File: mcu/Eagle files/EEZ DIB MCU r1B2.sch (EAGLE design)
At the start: 189 parts, among them IC1 TPD4E001DRLR, IC10 TPS2051BDBVR, IC11 TPS61169DCKR, IC12 TPD4E001DRLR, IC13 TPA6205A1DGN, IC14 TPD4E001DRLR, IC15 AR1021-I/SS, IC16 TPD4E001DRLR, IC17 DP83848CVV/NOPB, IC2 SN74LVC2G34DBVR, IC3 BTS3408G, IC4 STM32F769IGT6, IC5 LD1117ADT33TR, IC6 TPD4E001DRLR, IC7 TPD4E001DRLR, IC8 IS42S16400J, IC9 BR24G64FVT-3AGE2, J1 5033981892, Q1 MMBT5551, SW1 PEC16-2215F-S0024, SW2 BSF-3152, X1 ZL263-40DG, X2 ZL231-16KG, X3 1844249, X4 ZL231-20KG, X5 292304-1, X6 LMJTAB881243M-L, Y1 10MHz

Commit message: #3
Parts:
- removed X5: 292304-1, EEZ_Lib1:USB-B292304-1
- added J2: 678038020, EEZ_Lib1:678038020
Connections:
- net GND: now also J2.GND
- net PE: now also J2.SH1, J2.SH2; no longer X5.SHIELD
- net USB_D_N: now also J2.D-; no longer X5.2
- net USB_D_P: now also IC12.IO2, J2.D+; no longer IC12.IO3, X5.3
- net USB_OTG_FS_ID: now also IC12.IO3, J2.ID; no longer X5.4
- net USB_OTG_FS_VBUS: now also J2.VCC; no longer X5.1
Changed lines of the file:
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@@
 <?xml version="1.0" encoding="utf-8"?>
 <!DOCTYPE eagle SYSTEM "eagle.dtd">
-<eagle version="9.1.0">
+<eagle version="7.2.0">
 <drawing>
 <settings>
 <setting alwaysvectorfont="no"/>
-<setting keepoldvectorfont="yes"/>
 <setting verticaltext="up"/>
 </settings>
@@
 <part name="C22" library="rcl" deviceset="C-EU" device="C0603" value="N.C."/>
 <part name="SUPPLY3" library="supply2" deviceset="GND" device=""/>
-<part name="X5" library="EEZ_Lib1" deviceset="USB-B" device="292304-1" value="292304-1"/>
 <part name="PE3" library="supply1" deviceset="PE" device=""/>
 <part name="X1" library="EEZ_connectors" deviceset="ZL263-40DG" device="" value="ZL263-40DG"/>
@@
 <part name="+3V12" library="supply1" deviceset="+3V3" device=""/>
 <part name="+3V14" library="supply1" deviceset="+3V3" device=""/>
+<part name="J2" library="EEZ_Lib1" deviceset="678038020" device=""/>
+<part name="SUPPLY21" library="supply2" deviceset="GND" device=""/>
 </parts>
 <sheets>
@@
 <attribute name="DRAWING_NAME" x="180.34" y="19.05" size="2.54" layer="94" font="vector"/>
 </instance>
-<instance part="X5" gate="G$1" x="241.3" y="134.62" smashed="yes">
-<attribute name="NAME" x="243.84" y="137.795" size="1.778" layer="95"/>
-<attribute name="VALUE" x="250.19" y="121.92" size="1.778" layer="96"/>
-</instance>
-<instance part="PE3" gate="M" x="248.92" y="116.84" smashed="yes">
-<attribute name="VALUE" x="246.38" y="117.475" size="1.778" layer="96" rot="R180"/>
+<instance part="PE3" gate="M" x="243.84" y="111.76" smashed="yes">
+<attribute name="VALUE" x="241.3" y="112.395" size="1.778" layer="96" rot="R180"/>
 </instance>
 <instance part="IC11" gate="A" x="45.72" y="152.4" smashed="yes">
@@
 <attribute name="VALUE" x="248.031" y="143.51" size="1.778" layer="96" rot="MR180"/>
 </instance>
+<instance part="J2" gate="G$1" x="251.46" y="129.54" smashed="yes">
+<attribute name="NAME" x="251.46" y="139.065" size="1.778" layer="95"/>
+<attribute name="VALUE" x="246.38" y="113.665" size="1.778" layer="96"/>
+</instance>
+<instance part="SUPPLY21" gate="GND" x="236.22" y="119.38" smashed="yes">
+<attribute name="VALUE" x="233.68" y="115.57" size="1.778" layer="96"/>
+</instance>
 </instances>
 <busses>
@@
 <segment>
 <pinref part="PE3" gate="M" pin="PE"/>
-<pinref part="X5" gate="G$1" pin="SHIELD"/>
-<wire x1="248.92" y1="119.38" x2="248.92" y2="121.92" width="0.1524" layer="91"/>
+<wire x1="243.84" y1="114.3" x2="243.84" y2="116.84" width="0.1524" layer="91"/>
+<pinref part="J2" gate="G$1" pin="SH1"/>
+<wire x1="243.84" y1="116.84" x2="243.84" y2="119.38" width="0.1524" layer="91"/>
+<wire x1="246.38" y1="119.38" x2="243.84" y2="119.38" width="0.1524" layer="91"/>
+<pinref part="J2" gate="G$1" pin="SH2"/>
+<wire x1="246.38" y1="116.84" x2="243.84" y2="116.84" width="0.1524" layer="91"/>
+<junction x="243.84" y="116.84"/>
 </segment>
 </net>
@@
 <pinref part="SUPPLY46" gate="GND" pin="GND"/>
 </segment>
+<segment>
+<pinref part="J2" gate="G$1" pin="GND"/>
+<wire x1="246.38" y1="124.46" x2="236.22" y2="124.46" width="0.1524" layer="91"/>
+<wire x1="236.22" y1="124.46" x2="236.22" y2="121.92" width="0.1524" layer="91"/>
+<pinref part="SUPPLY21" gate="GND" pin="GND"/>
+</segment>
 </net>
 <net name="VLED+" class="0">
@@
 <wire x1="187.96" y1="134.62" x2="218.44" y2="134.62" width="0.1524" layer="91"/>
 <wire x1="218.44" y1="134.62" x2="236.22" y2="134.62" width="0.1524" layer="91"/>
-<wire x1="236.22" y1="134.62" x2="241.3" y2="134.62" width="0.1524" layer="91"/>
 <wire x1="210.82" y1="160.02" x2="218.44" y2="160.02" width="0.1524" layer="91"/>
 <wire x1="218.44" y1="160.02" x2="218.44" y2="134.62" width="0.1524" layer="91"/>
@@
 <pinref part="C49" gate="G$1" pin="2"/>
 <junction x="187.96" y="114.3"/>
-<pinref part="X5" gate="G$1" pin="1"/>
+<pinref part="J2" gate="G$1" pin="VCC"/>
+<wire x1="236.22" y1="134.62" x2="246.38" y2="134.62" width="0.1524" layer="91"/>
 </segment>
 </net>
@@
 <segment>
 <label x="167.64" y="127.635" size="1.27" layer="102"/>
-<wire x1="167.64" y1="127" x2="241.3" y2="127" width="0.1524" layer="91"/>
-<pinref part="X5" gate="G$1" pin="4"/>
+<wire x1="167.64" y1="127" x2="223.52" y2="127" width="0.1524" layer="91"/>
+<pinref part="J2" gate="G$1" pin="ID"/>
+<wire x1="223.52" y1="127" x2="246.38" y2="127" width="0.1524" layer="91"/>
+<pinref part="IC12" gate="G$1" pin="IO3"/>
+<wire x1="215.9" y1="109.22" x2="223.52" y2="109.22" width="0.1524" layer="91"/>
+<wire x1="223.52" y1="109.22" x2="223.52" y2="127" width="0.1524" layer="91"/>
+<junction x="223.52" y="127"/>
 </segment>
 </net>
@@
 <segment>
 <pinref part="R34" gate="G$1" pin="1"/>
-<wire x1="203.2" y1="129.54" x2="220.98" y2="129.54" width="0.1524" layer="91"/>
 <label x="229.235" y="130.175" size="1.27" layer="102"/>
-<pinref part="X5" gate="G$1" pin="3"/>
-<pinref part="IC12" gate="G$1" pin="IO3"/>
-<wire x1="220.98" y1="129.54" x2="241.3" y2="129.54" width="0.1524" layer="91"/>
-<wire x1="215.9" y1="109.22" x2="220.98" y2="109.22" width="0.1524" layer="91"/>
-<wire x1="220.98" y1="109.22" x2="220.98" y2="129.54" width="0.1524" layer="91"/>
+<wire x1="203.2" y1="129.54" x2="220.98" y2="129.54" width="0.1524" layer="91"/>
+<pinref part="J2" gate="G$1" pin="D+"/>
+<wire x1="220.98" y1="129.54" x2="246.38" y2="129.54" width="0.1524" layer="91"/>
+<pinref part="IC12" gate="G$1" pin="IO2"/>
+<wire x1="215.9" y1="111.76" x2="220.98" y2="111.76" width="0.1524" layer="91"/>
+<wire x1="220.98" y1="111.76" x2="220.98" y2="129.54" width="0.1524" layer="91"/>
 <junction x="220.98" y="129.54"/>
 </segment>
@@
 <pinref part="R33" gate="G$1" pin="1"/>
 <label x="229.235" y="132.715" size="1.27" layer="102"/>
-<pinref part="X5" gate="G$1" pin="2"/>
 <wire x1="203.2" y1="132.08" x2="218.44" y2="132.08" width="0.1524" layer="91"/>
-<wire x1="218.44" y1="132.08" x2="241.3" y2="132.08" width="0.1524" layer="91"/>
+<wire x1="218.44" y1="132.08" x2="246.38" y2="132.08" width="0.1524" layer="91"/>
 <pinref part="IC12" gate="G$1" pin="IO1"/>
 <wire x1="215.9" y1="114.3" x2="218.44" y2="114.3" width="0.1524" layer="91"/>
 <wire x1="218.44" y1="114.3" x2="218.44" y2="132.08" width="0.1524" layer="91"/>
 <junction x="218.44" y="132.08"/>
+<pinref part="J2" gate="G$1" pin="D-"/>
 </segment>
 </net>

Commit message: #4
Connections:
- net +3V3: no longer C45.1, L2.1, R28.1
- net +5V: now also C45.1, L2.1, R28.1
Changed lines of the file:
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@@
 <?xml version="1.0" encoding="utf-8"?>
 <!DOCTYPE eagle SYSTEM "eagle.dtd">
-<eagle version="7.2.0">
+<eagle version="6.1">
 <drawing>
 <settings>
@@
 <part name="+3V316" library="supply1" deviceset="+3V3" device=""/>
 <part name="D2" library="EEZ_Lib1" deviceset="SCHOTTKY" device="SOD123" value="NSR0240"/>
-<part name="+3V313" library="supply1" deviceset="+3V3" device=""/>
 <part name="+3V315" library="supply1" deviceset="+3V3" device=""/>
 <part name="R35" library="rcl" deviceset="R-EU_" device="R0805" value="10K"/>
@@
 <part name="J2" library="EEZ_Lib1" deviceset="678038020" device=""/>
 <part name="SUPPLY21" library="supply2" deviceset="GND" device=""/>
+<part name="P+9" library="supply1" deviceset="+5V" device=""/>
 </parts>
 <sheets>
@@
 <attribute name="VALUE" x="70.866" y="166.751" size="1.778" layer="96" rot="MR0"/>
 </instance>
-<instance part="+3V313" gate="G$1" x="17.78" y="170.18" smashed="yes" rot="MR270">
-<attribute name="VALUE" x="17.145" y="169.545" size="1.778" layer="96" rot="MR0"/>
-</instance>
 <instance part="+3V315" gate="G$1" x="63.5" y="106.68" smashed="yes" rot="R90">
 <attribute name="VALUE" x="60.96" y="108.585" size="1.778" layer="96"/>
@@
 <attribute name="VALUE" x="233.68" y="115.57" size="1.778" layer="96"/>
 </instance>
+<instance part="P+9" gate="1" x="17.78" y="170.18" smashed="yes" rot="MR270">
+<attribute name="VALUE" x="17.145" y="169.545" size="1.778" layer="96" rot="MR0"/>
+</instance>
 </instances>
 <busses>
@@
 </segment>
 <segment>
-<pinref part="L2" gate="G$1" pin="1"/>
-<wire x1="22.86" y1="167.64" x2="22.86" y2="170.18" width="0.1524" layer="91"/>
-<wire x1="22.86" y1="170.18" x2="30.48" y2="170.18" width="0.1524" layer="91"/>
-<pinref part="C45" gate="G$1" pin="1"/>
-<pinref part="R28" gate="G$1" pin="1"/>
-<wire x1="30.48" y1="170.18" x2="40.64" y2="170.18" width="0.1524" layer="91"/>
-<wire x1="30.48" y1="167.64" x2="30.48" y2="170.18" width="0.1524" layer="91"/>
-<junction x="30.48" y="170.18"/>
-<wire x1="22.86" y1="170.18" x2="20.32" y2="170.18" width="0.1524" layer="91"/>
-<junction x="22.86" y="170.18"/>
-<pinref part="+3V313" gate="G$1" pin="+3V3"/>
-</segment>
-<segment>
 <pinref part="IC14" gate="G$1" pin="VCC"/>
 <wire x1="40.64" y1="60.96" x2="38.1" y2="60.96" width="0.1524" layer="91"/>
@@
 <pinref part="P+4" gate="1" pin="+5V"/>
 </segment>
+<segment>
+<pinref part="L2" gate="G$1" pin="1"/>
+<wire x1="22.86" y1="167.64" x2="22.86" y2="170.18" width="0.1524" layer="91"/>
+<wire x1="22.86" y1="170.18" x2="30.48" y2="170.18" width="0.1524" layer="91"/>
+<pinref part="C45" gate="G$1" pin="1"/>
+<pinref part="R28" gate="G$1" pin="1"/>
+<wire x1="30.48" y1="170.18" x2="40.64" y2="170.18" width="0.1524" layer="91"/>
+<wire x1="30.48" y1="167.64" x2="30.48" y2="170.18" width="0.1524" layer="91"/>
+<junction x="30.48" y="170.18"/>
+<wire x1="22.86" y1="170.18" x2="20.32" y2="170.18" width="0.1524" layer="91"/>
+<junction x="22.86" y="170.18"/>
+<pinref part="P+9" gate="1" pin="+5V"/>
+</segment>
 </net>
 <net name="!USB_OTG_FS_OC" class="0">
@@
 </schematic>
 </drawing>
-<compatibility>
-<note version="6.3" minversion="6.2.2" severity="warning">
-Since Version 6.2.2 text objects can contain more than one line,
-which will not be processed correctly with this version.
-</note>
-</compatibility>
 </eagle>

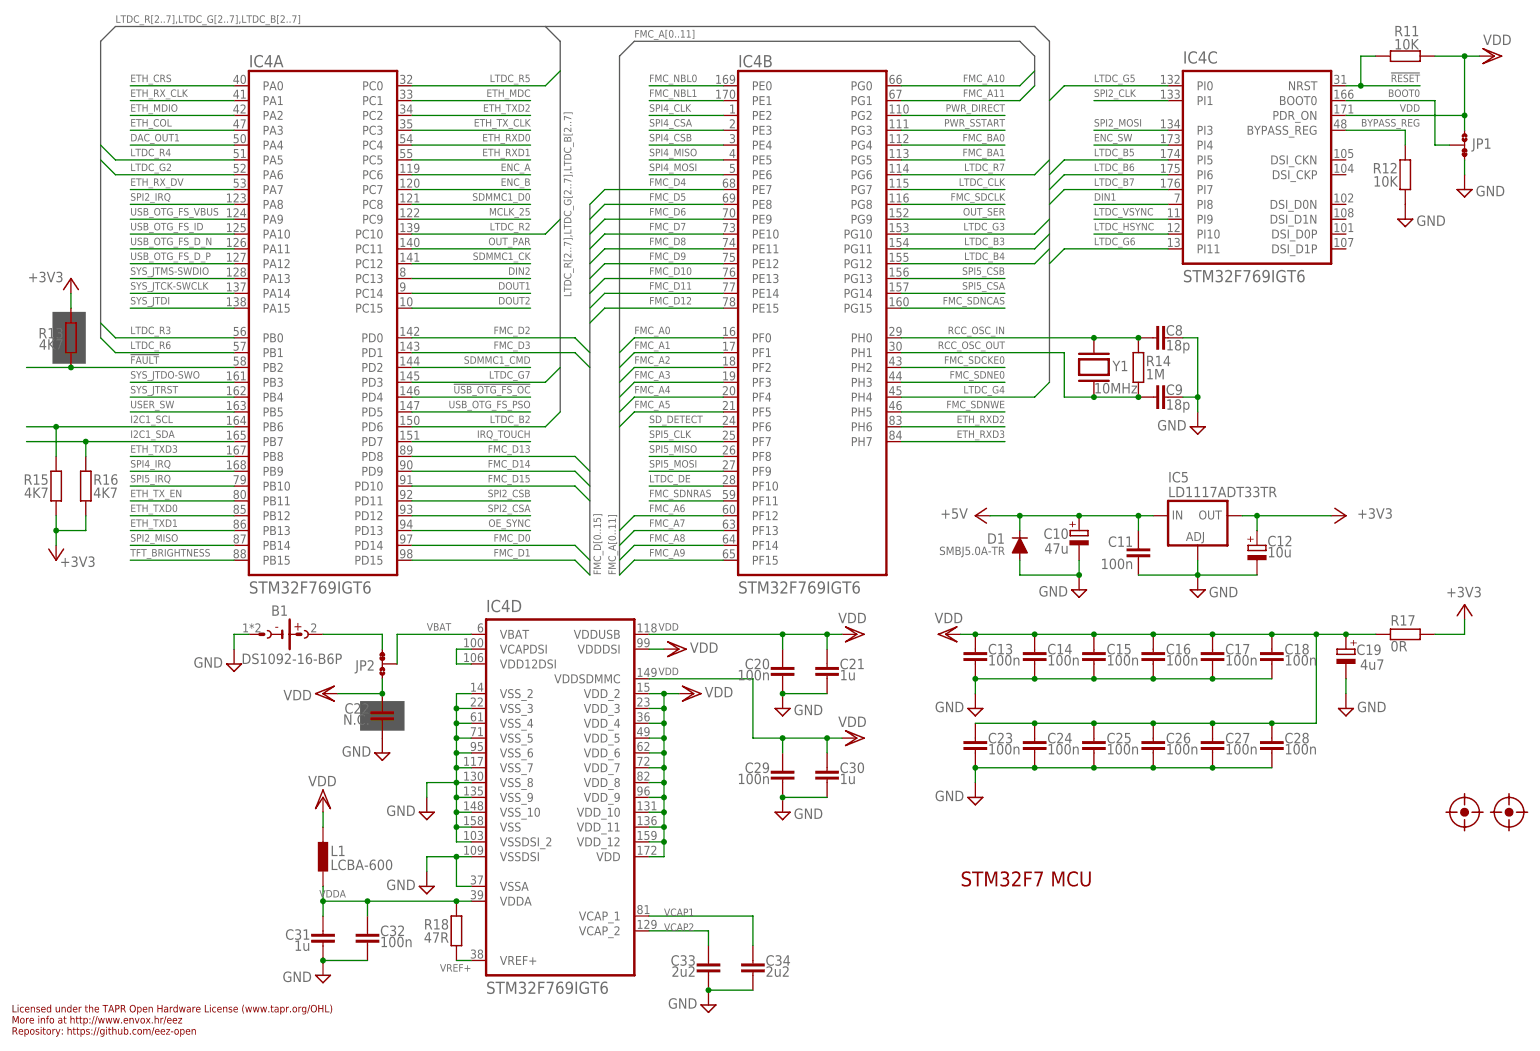
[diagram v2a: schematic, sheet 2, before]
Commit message: PCB parts images added
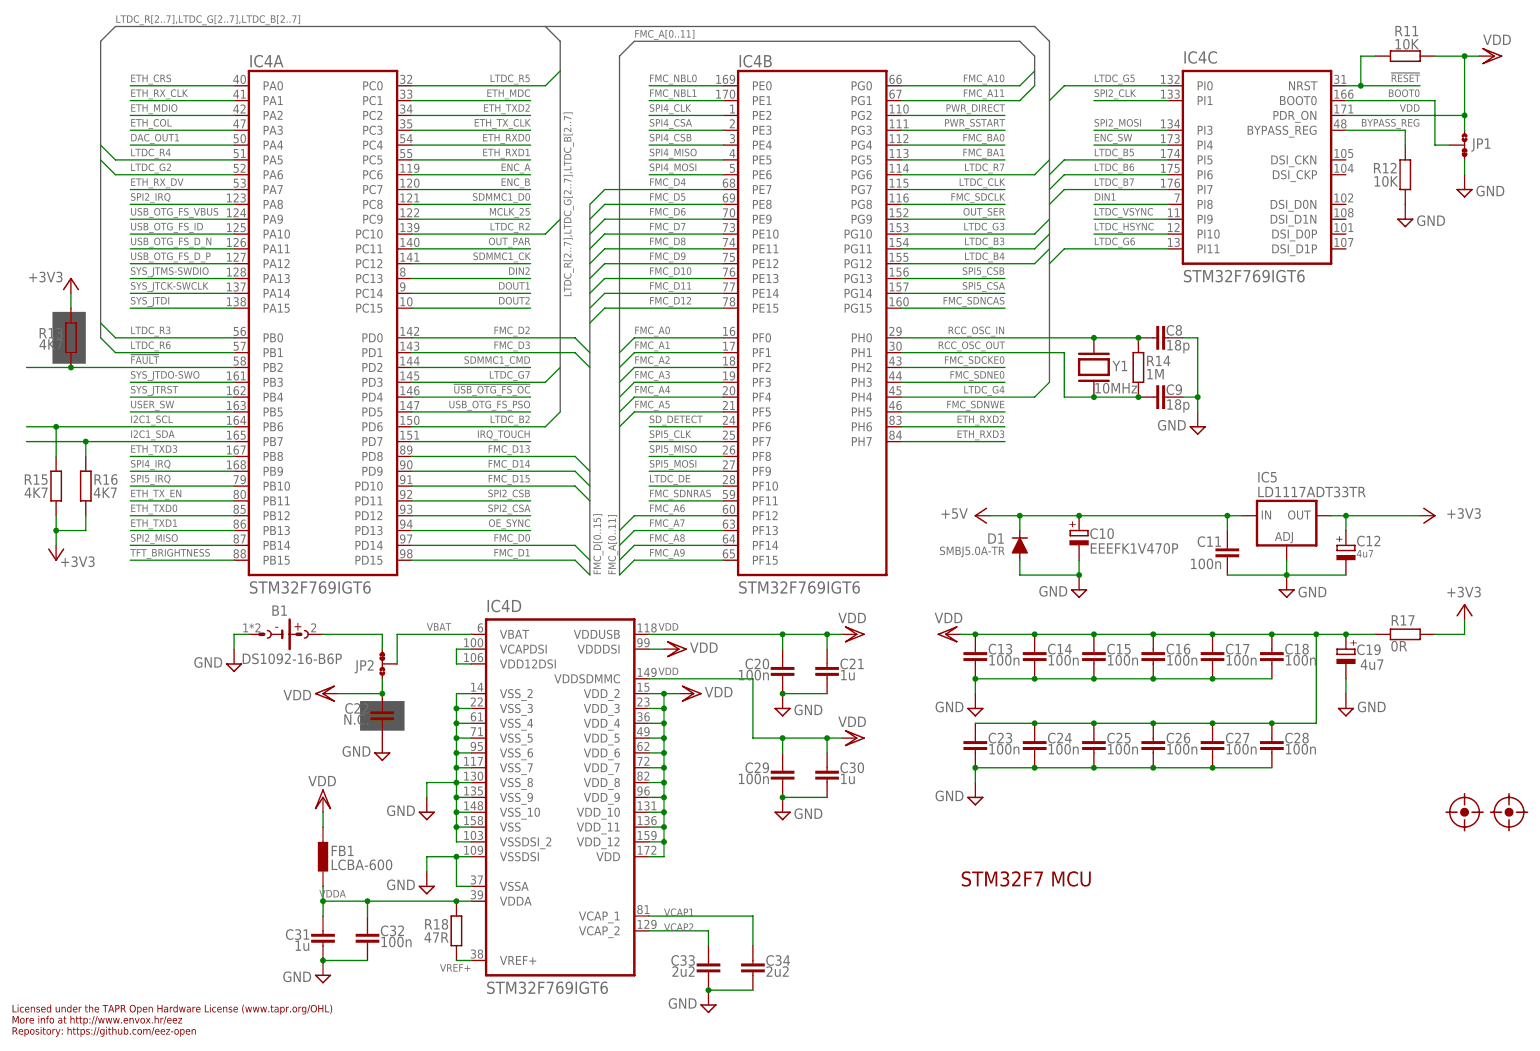
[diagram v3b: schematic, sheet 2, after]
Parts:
- removed L2: DLG-0403-4R7, EEZ_Lib1:DE0403
- added FB2: LCBA-600, EEZ_Lib1:FERRITE_BEAD0603
- C10: value 47u -> EEEFK1V470P
- C12: value 10u -> 4u7
- C47: value 4u7/16V (293D475X9016A2TE3) -> 4u7
- D2: value NSR0240 -> RB751V40T1G or NSR0240
- FB1: value 60R@100MHz -> LCBA-600
- J1: value 5033981892 -> 503398-1892
- J2: value 678038020 -> 67803-8020
- L1: value LCBA-600 -> DLG-0403-4R7; device EEZ_Lib1:FERRITE_BEAD0603 -> EEZ_Lib1:DE0403
- SW2: value BSF-3152 -> B3F-3152; device EEZ_switches:BSF-315X -> EEZ_switches:B3F-315X
- renumbered X6 to X5
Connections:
- net +3V3: now also FB2.1; no longer FB1.1
- net +3V3(A): now also FB2.2; no longer FB1.2
- net +5V: now also L1.1; no longer L2.1
- net SW_WLED: now also L1.2; no longer L2.2
- net VDD: now also FB1.1; no longer L1.1
- net VDDA: now also FB1.2; no longer L1.2
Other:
- moved on the sheet: C11, C12, IC5, SP1

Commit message: minor changes in BOMs
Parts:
- C37: device rcl:C-EUC1210 -> rcl:C-EUC1206
- C56: value 220n -> 470n
- SPEED: value HSMY-C170 -> LTST-C170YKT
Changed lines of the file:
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@@
 <part name="C60" library="rcl" deviceset="C-EU" device="C0603" value="100n"/>
 <part name="C62" library="rcl" deviceset="C-EU" device="C0603" value="100n"/>
-<part name="SPEED" library="EEZ_Lib1" deviceset="LED" device="0805" value="HSMY-C170"/>
+<part name="SPEED" library="EEZ_Lib1" deviceset="LED" device="0805" value="LTST-C170YKT"/>
 <part name="R47" library="rcl" deviceset="R-EU_" device="R0805" value="2K2"/>
 <part name="R50" library="rcl" deviceset="R-EU_" device="R0805" value="220R"/>
@@
 <part name="+3V34" library="supply1" deviceset="+3V3" device=""/>
 <part name="+3V312" library="supply1" deviceset="+3V3" device=""/>
-<part name="C37" library="rcl" deviceset="C-EU" device="C1210" value="10u"/>
+<part name="C37" library="rcl" deviceset="C-EU" device="C1206" value="10u"/>
 <part name="SUPPLY26" library="supply2" deviceset="GND" device=""/>
 <part name="SUPPLY18" library="supply2" deviceset="GND" device=""/>
@@
 <part name="R36" library="rcl" deviceset="R-EU_" device="R0805" value="20K"/>
 <part name="R37" library="rcl" deviceset="R-EU_" device="R0805" value="10K"/>
-<part name="C56" library="rcl" deviceset="C-EU" device="C0805" value="220n"/>
+<part name="C56" library="rcl" deviceset="C-EU" device="C0805" value="470n"/>
 <part name="C51" library="rcl" deviceset="C-EU" device="C0805" value="470n"/>
 <part name="R40" library="rcl" deviceset="R-EU_" device="R0805" value="47K"/>
@@
 <rectangle x1="186.69" y1="142.875" x2="194.31" y2="146.685" layer="97" rot="R180"/>
 <text x="226.06" y="151.13" size="1.27" layer="103" rot="MR180">Tant.</text>
+<rectangle x1="192.405" y1="46.99" x2="199.39" y2="56.515" layer="97"/>
 </plain>
 <instances>
